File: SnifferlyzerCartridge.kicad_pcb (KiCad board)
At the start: 2 copper layers, 64.8 x 55.9 mm, 11 parts, among them J1 Cartridge Connector, J2 Conn_01x10_Male, J3 Conn_01x10_Male, U1 W25Q128, U2 74LCX16245

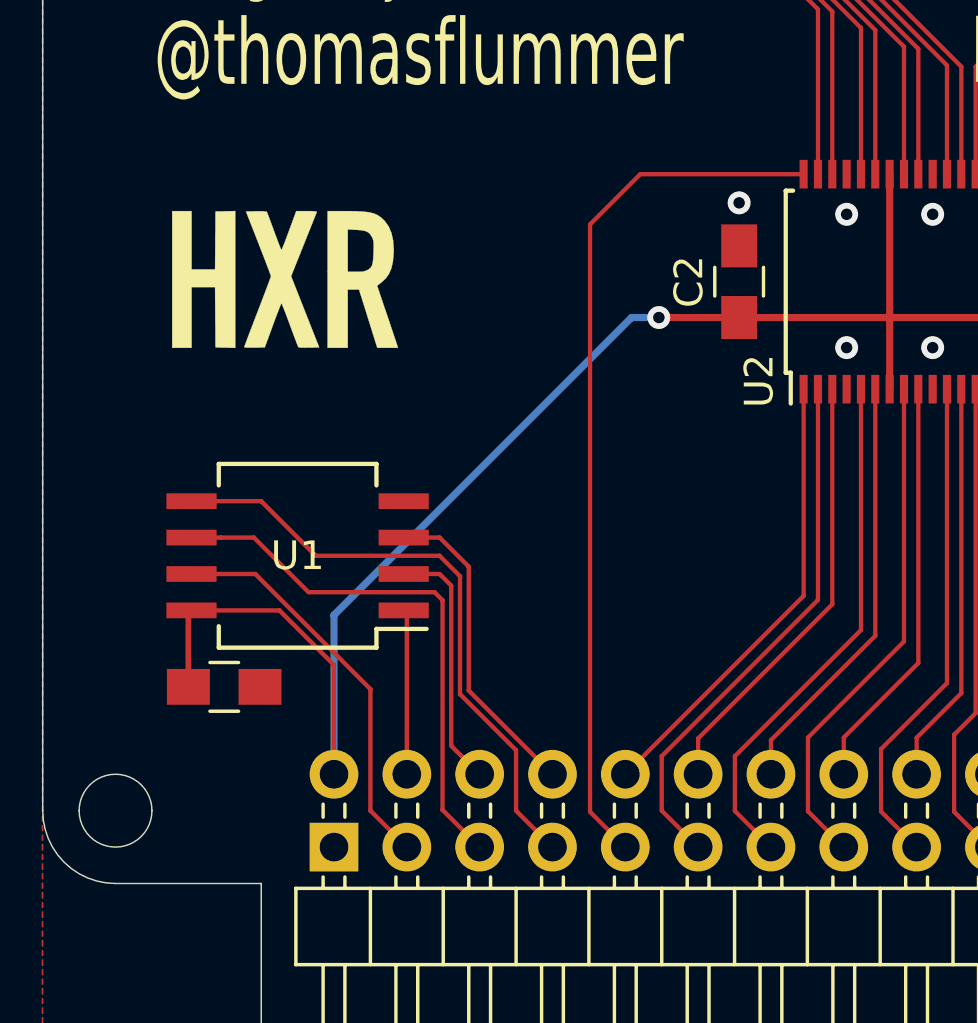
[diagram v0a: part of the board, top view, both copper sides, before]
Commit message: Fixed error in cartridge connector pin assignments
Updated to version 1.2
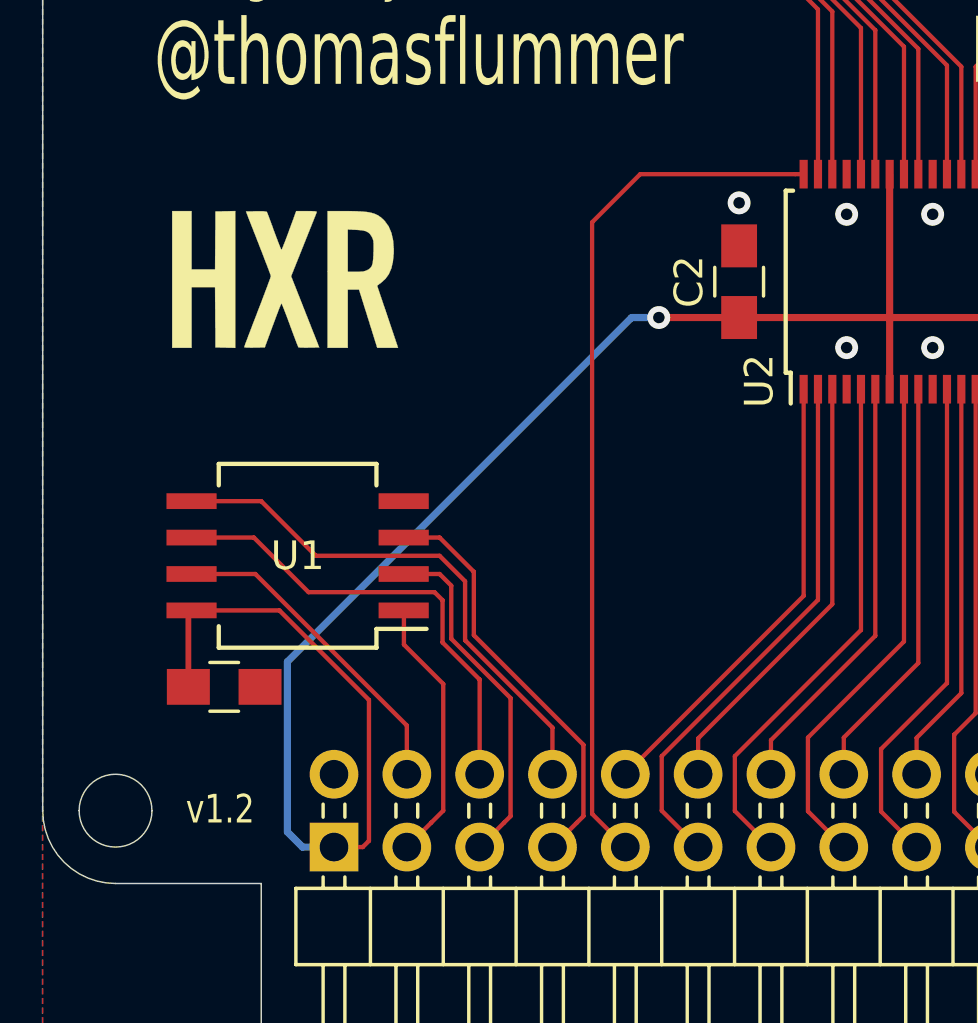
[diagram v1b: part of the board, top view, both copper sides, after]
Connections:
- J1 pad 1: GND -> +3V3
- J1 pad 2: +3V3 -> GND
- J1 pad 3: F_HOLD -> F_CS
- J1 pad 39: +5V -> +BATT
- J1 pad 4: F_CS -> F_HOLD
- J1 pad 40: +BATT -> +5V
- J1 pad 5: F_SCK -> F_MISO
- J1 pad 6: F_MISO -> F_SCK
- J1 pad 7: F_MOSI -> F_WP
- J1 pad 8: F_WP -> F_MOSI
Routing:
- net +3V3: track 67.3 -> 75.9 mm
- net F_CS: track 5.76 -> 9.51 mm
- net F_MISO: track 8.82 -> 12.3 mm
- net F_WP: track 11.1 -> 14.6 mm
- net F_MOSI: track 21.2 -> 18.7 mm
- net F_HOLD: track 13.9 -> 11.4 mm
- net F_SCK: track 18.8 -> 16.3 mm
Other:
- board text added: "v1.2"
